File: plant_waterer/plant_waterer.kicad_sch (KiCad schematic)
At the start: 26 parts, among them J1 Conn_01x02, J2 Conn_01x02, J3 PJ-002AH, J4 Conn_01x03, U1 TB6612FNG,C,8,EL, U2 OLED_DISP, U3 XIAO_RP2040, U4 ESD7002, U5 AP2204R-5.0TRG1

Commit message: Switched pot to ADC pin
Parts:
- removed R1: 10K, Resistor_SMD:R_0805_2012Metric_Pad1.20x1.40mm_HandSolder, symbol Device:R
- removed RV1: 100K, Connector_PinHeader_2.54mm:PinHeader_1x03_P2.54mm_Vertical, symbol Device:Varistor
- added RV1: R_Potentiometer, Potentiometer_THT:Potentiometer_Bourns_3266Y_Vertical, symbol Device:R_Potentiometer
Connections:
- net +3.3V: now also RV1.1
- net GND: now also RV1.3
- net PWMA: now also U3.7 (CSn); no longer U3.1 (A1)
- new net: RV1.2, U3.1 (A1)
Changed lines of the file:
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@@
   (junction (at 90.17 48.26) (diameter 0) (color 0 0 0 0)
   )
-  (junction (at 115.57 137.16) (diameter 0) (color 0 0 0 0)
-  )
   (junction (at 250.19 102.87) (diameter 0) (color 0 0 0 0)
   )
@@
     (stroke (width 0) (type default) (color 0 0 0 0))
   )
-  (wire (pts (xy 107.95 133.35) (xy 107.95 137.16))
-    (stroke (width 0) (type default) (color 0 0 0 0))
-  )
   (wire (pts (xy 96.52 48.26) (xy 105.41 48.26))
     (stroke (width 0) (type default) (color 0 0 0 0))
@@
     (stroke (width 0) (type default) (color 0 0 0 0))
   )
-  (wire (pts (xy 115.57 148.59) (xy 115.57 151.13))
+  (wire (pts (xy 115.57 133.35) (xy 115.57 135.89))
     (stroke (width 0) (type default) (color 0 0 0 0))
   )
@@
     (stroke (width 0) (type default) (color 0 0 0 0))
   )
+  (wire (pts (xy 111.76 129.54) (xy 110.49 129.54))
+    (stroke (width 0) (type default) (color 0 0 0 0))
+  )
   (wire (pts (xy 148.59 29.21) (xy 148.59 31.75))
     (stroke (width 0) (type default) (color 0 0 0 0))
@@
     (stroke (width 0) (type default) (color 0 0 0 0))
   )
+  (wire (pts (xy 78.74 120.65) (xy 78.74 137.16))
+    (stroke (width 0) (type default) (color 0 0 0 0))
+  )
   (wire (pts (xy 54.61 31.75) (xy 59.69 31.75))
     (stroke (width 0) (type default) (color 0 0 0 0))
@@
     (stroke (width 0) (type default) (color 0 0 0 0))
   )
-  (wire (pts (xy 115.57 133.35) (xy 115.57 137.16))
+  (wire (pts (xy 110.49 129.54) (xy 110.49 137.16))
     (stroke (width 0) (type default) (color 0 0 0 0))
   )
@@
     (stroke (width 0) (type default) (color 0 0 0 0))
   )
+  (wire (pts (xy 110.49 137.16) (xy 78.74 137.16))
+    (stroke (width 0) (type default) (color 0 0 0 0))
+  )
   (polyline (pts (xy 158.75 87.63) (xy 264.16 87.63))
     (stroke (width 0) (type default) (color 0 0 0 0))
@@
     (stroke (width 0) (type default) (color 0 0 0 0))
   )
-  (wire (pts (xy 102.87 133.35) (xy 107.95 133.35))
-    (stroke (width 0) (type default) (color 0 0 0 0))
-  )
   (wire (pts (xy 43.18 31.75) (xy 43.18 35.56))
     (stroke (width 0) (type default) (color 0 0 0 0))
@@
     (stroke (width 0) (type default) (color 0 0 0 0))
   )
-  (wire (pts (xy 115.57 137.16) (xy 115.57 140.97))
-    (stroke (width 0) (type default) (color 0 0 0 0))
-  )
   (wire (pts (xy 90.17 48.26) (xy 96.52 48.26))
     (stroke (width 0) (type default) (color 0 0 0 0))
@@
     (stroke (width 0) (type default) (color 0 0 0 0))
   )
-  (wire (pts (xy 107.95 137.16) (xy 115.57 137.16))
-    (stroke (width 0) (type default) (color 0 0 0 0))
-  )
   (wire (pts (xy 256.54 115.57) (xy 256.54 116.84))
     (stroke (width 0) (type default) (color 0 0 0 0))
@@
     (stroke (width 0) (type default) (color 0 0 0 0))
   )
-  (wire (pts (xy 81.28 120.65) (xy 87.63 120.65))
+  (wire (pts (xy 78.74 120.65) (xy 87.63 120.65))
     (stroke (width 0) (type default) (color 0 0 0 0))
   )
@@
     (stroke (width 0) (type default) (color 0 0 0 0))
   )
+  (wire (pts (xy 102.87 133.35) (xy 104.14 133.35))
+    (stroke (width 0) (type default) (color 0 0 0 0))
+  )
   (wire (pts (xy 39.37 31.75) (xy 43.18 31.75))
     (stroke (width 0) (type default) (color 0 0 0 0))
@@
     (effects (font (size 1.27 1.27)) (justify left bottom))
   )
-  (label "PWMA" (at 81.28 120.65 0)
-    (effects (font (size 1.27 1.27)) (justify left bottom))
-  )
   (label "AIN2" (at 104.14 128.27 0)
     (effects (font (size 1.27 1.27)) (justify left bottom))
@@
   )
   (label "BIN1" (at 81.28 123.19 0)
+    (effects (font (size 1.27 1.27)) (justify left bottom))
+  )
+  (label "PWMA" (at 104.14 133.35 0)
     (effects (font (size 1.27 1.27)) (justify left bottom))
   )
@@
     (pin "1")
   )
+  (symbol (lib_id "Device:R_Potentiometer") (at 115.57 129.54 0) (mirror y) (unit 1)
+    (in_bom yes) (on_board yes)
+    (property "Reference" "RV1" (id 0) (at 118.11 128.2699 0)
+      (effects (font (size 1.27 1.27)) (justify right))
+    )
+    (property "Value" "R_Potentiometer" (id 1) (at 116.84 137.16 0)
+      (effects (font (size 1.27 1.27)) (justify right) hide)
+    )
+    (property "Footprint" "Potentiometer_THT:Potentiometer_Bourns_3266Y_Vertical" (id 2) (at 115.57 129.54 0)
+      (effects (font (size 1.27 1.27)) hide)
+    )
+    (property "Datasheet" "~" (id 3) (at 115.57 129.54 0)
+      (effects (font (size 1.27 1.27)) hide)
+    )
+    (pin "1")
+    (pin "2")
+    (pin "3")
+  )
   (symbol (lib_id "power:GND") (at 78.74 154.94 0) (unit 1)
     (in_bom yes) (on_board yes) (fields_autoplaced)
@@
     )
     (pin "1")
-  )
-  (symbol (lib_id "Device:R") (at 115.57 144.78 0) (unit 1)
-    (in_bom yes) (on_board yes) (fields_autoplaced)
-    (property "Reference" "R1" (id 0) (at 118.11 143.5099 0)
-      (effects (font (size 1.27 1.27)) (justify left))
-    )
-    (property "Value" "10K" (id 1) (at 118.11 146.0499 0)
-      (effects (font (size 1.27 1.27)) (justify left))
-    )
-    (property "Footprint" "Resistor_SMD:R_0805_2012Metric_Pad1.20x1.40mm_HandSolder" (id 2) (at 113.792 144.78 90)
-      (effects (font (size 1.27 1.27)) hide)
-    )
-    (property "Datasheet" "~" (id 3) (at 115.57 144.78 0)
-      (effects (font (size 1.27 1.27)) hide)
-    )
-    (pin "1")
-    (pin "2")
   )
   (symbol (lib_id "Device:C") (at 83.82 38.1 180) (unit 1)
@@
     (pin "1")
   )
-  (symbol (lib_id "power:GND") (at 115.57 151.13 0) (unit 1)
-    (in_bom yes) (on_board yes) (fields_autoplaced)
-    (property "Reference" "#PWR0105" (id 0) (at 115.57 157.48 0)
-      (effects (font (size 1.27 1.27)) hide)
-    )
-    (property "Value" "GND" (id 1) (at 115.57 156.21 0))
-    (property "Footprint" "" (id 2) (at 115.57 151.13 0)
-      (effects (font (size 1.27 1.27)) hide)
-    )
-    (property "Datasheet" "" (id 3) (at 115.57 151.13 0)
-      (effects (font (size 1.27 1.27)) hide)
-    )
-    (pin "1")
-  )
-  (symbol (lib_id "Device:Varistor") (at 115.57 129.54 0) (unit 1)
-    (in_bom yes) (on_board yes) (fields_autoplaced)
-    (property "Reference" "RV1" (id 0) (at 118.11 128.5231 0)
-      (effects (font (size 1.27 1.27)) (justify left))
-    )
-    (property "Value" "100K" (id 1) (at 118.11 131.0631 0)
-      (effects (font (size 1.27 1.27)) (justify left))
-    )
-    (property "Footprint" "Connector_PinHeader_2.54mm:PinHeader_1x03_P2.54mm_Vertical" (id 2) (at 113.792 129.54 90)
-      (effects (font (size 1.27 1.27)) hide)
-    )
-    (property "Datasheet" "~" (id 3) (at 115.57 129.54 0)
-      (effects (font (size 1.27 1.27)) hide)
-    )
-    (pin "1")
-    (pin "2")
+  (symbol (lib_id "power:GND") (at 115.57 135.89 0) (unit 1)
+    (in_bom yes) (on_board yes) (fields_autoplaced)
+    (property "Reference" "#PWR0105" (id 0) (at 115.57 142.24 0)
+      (effects (font (size 1.27 1.27)) hide)
+    )
+    (property "Value" "GND" (id 1) (at 115.57 140.97 0))
+    (property "Footprint" "" (id 2) (at 115.57 135.89 0)
+      (effects (font (size 1.27 1.27)) hide)
+    )
+    (property "Datasheet" "" (id 3) (at 115.57 135.89 0)
+      (effects (font (size 1.27 1.27)) hide)
+    )
+    (pin "1")
   )
   (symbol (lib_id "Device:R") (at 68.58 123.19 0) (unit 1)
@@
       (reference "JP1") (unit 1) (value "Jumper_2_Bridged") (footprint "Connector_PinHeader_2.54mm:PinHeader_1x02_P2.54mm_Vertical")
     )
-    (path "/3db4251a-e88f-41da-b4ca-02be30b2764f"
-      (reference "R1") (unit 1) (value "10K") (footprint "Resistor_SMD:R_0805_2012Metric_Pad1.20x1.40mm_HandSolder")
-    )
     (path "/12cb9a3a-0dce-4456-8425-08803bf20070"
       (reference "R2") (unit 1) (value "10K") (footprint "Resistor_SMD:R_0805_2012Metric_Pad1.20x1.40mm_HandSolder")
@@
       (reference "R3") (unit 1) (value "10K") (footprint "Resistor_SMD:R_0805_2012Metric_Pad1.20x1.40mm_HandSolder")
     )
-    (path "/b008a221-6b1c-4862-b6b9-3bd19966dc9e"
-      (reference "RV1") (unit 1) (value "100K") (footprint "Connector_PinHeader_2.54mm:PinHeader_1x03_P2.54mm_Vertical")
+    (path "/2dee0ead-6279-42da-9328-a22cafe0f3c3"
+      (reference "RV1") (unit 1) (value "R_Potentiometer") (footprint "Potentiometer_THT:Potentiometer_Bourns_3266Y_Vertical")
     )
     (path "/032b3c9e-8639-45d6-8bdd-7a89ce998692"

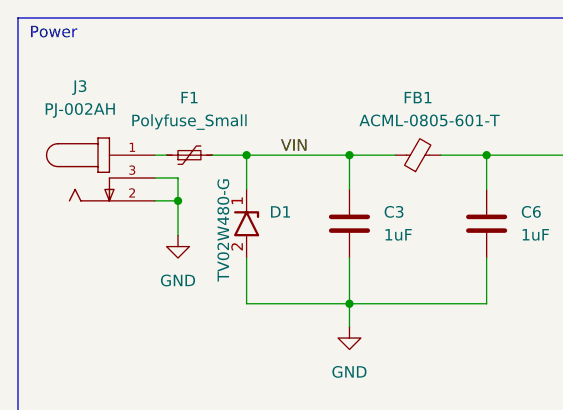
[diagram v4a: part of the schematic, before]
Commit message: V7 pre-switch to RPi-Pico
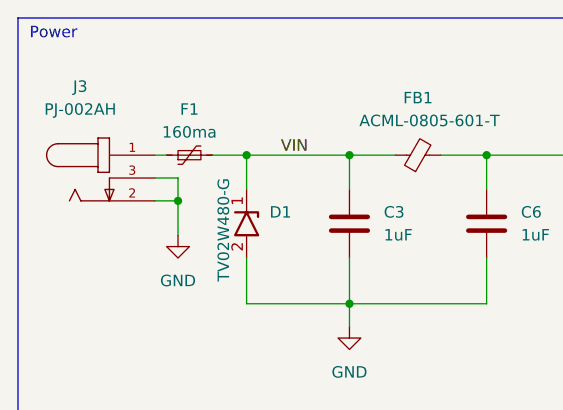
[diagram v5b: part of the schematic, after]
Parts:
- F1: value Polyfuse_Small -> 160ma

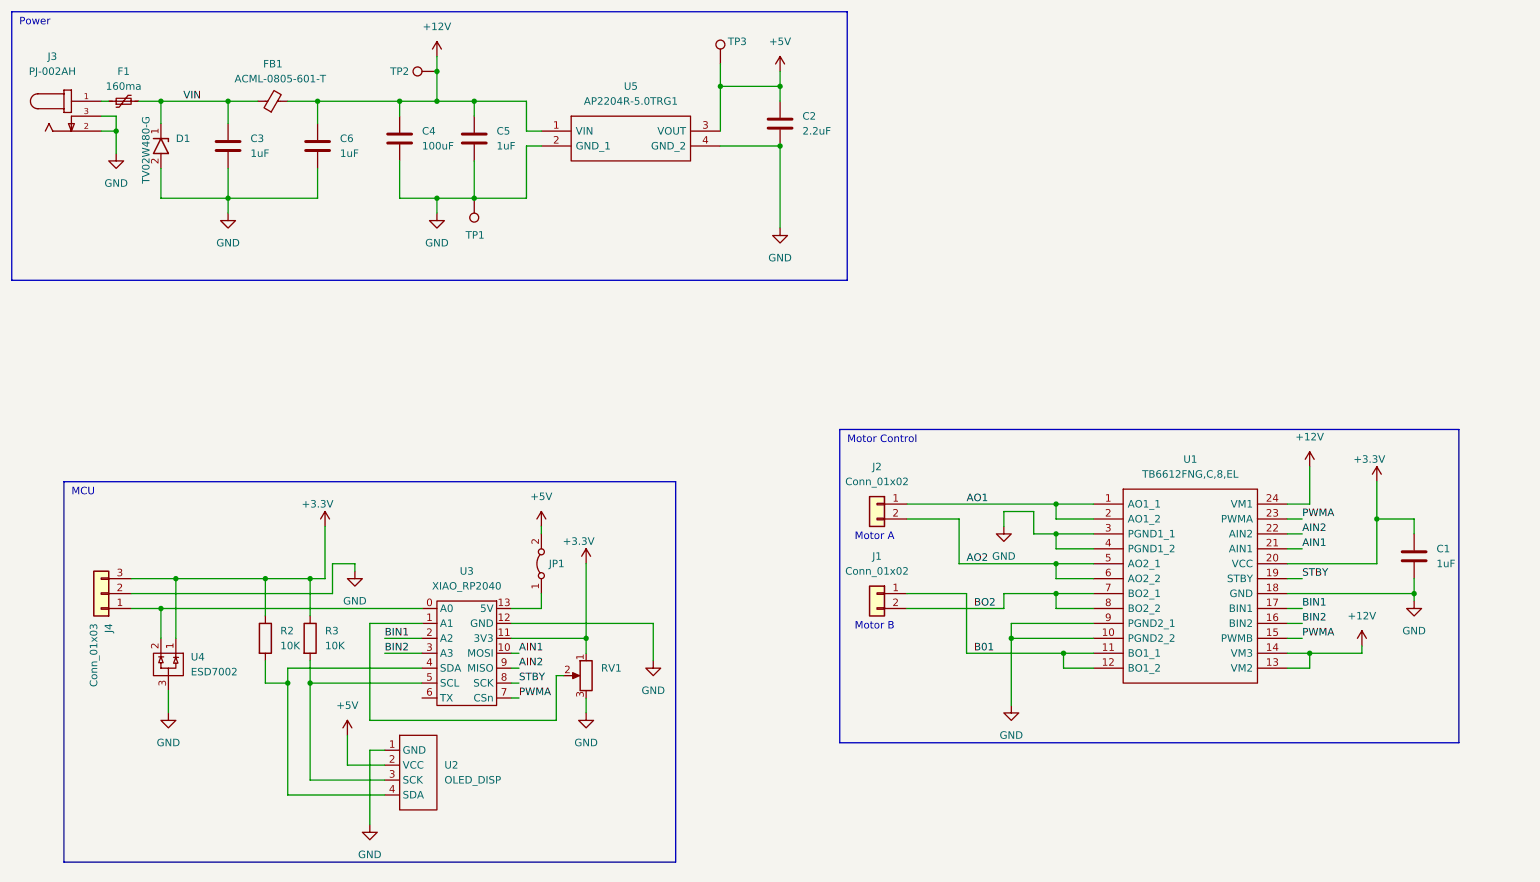
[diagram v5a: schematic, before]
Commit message: Swapped in RPi Pico W
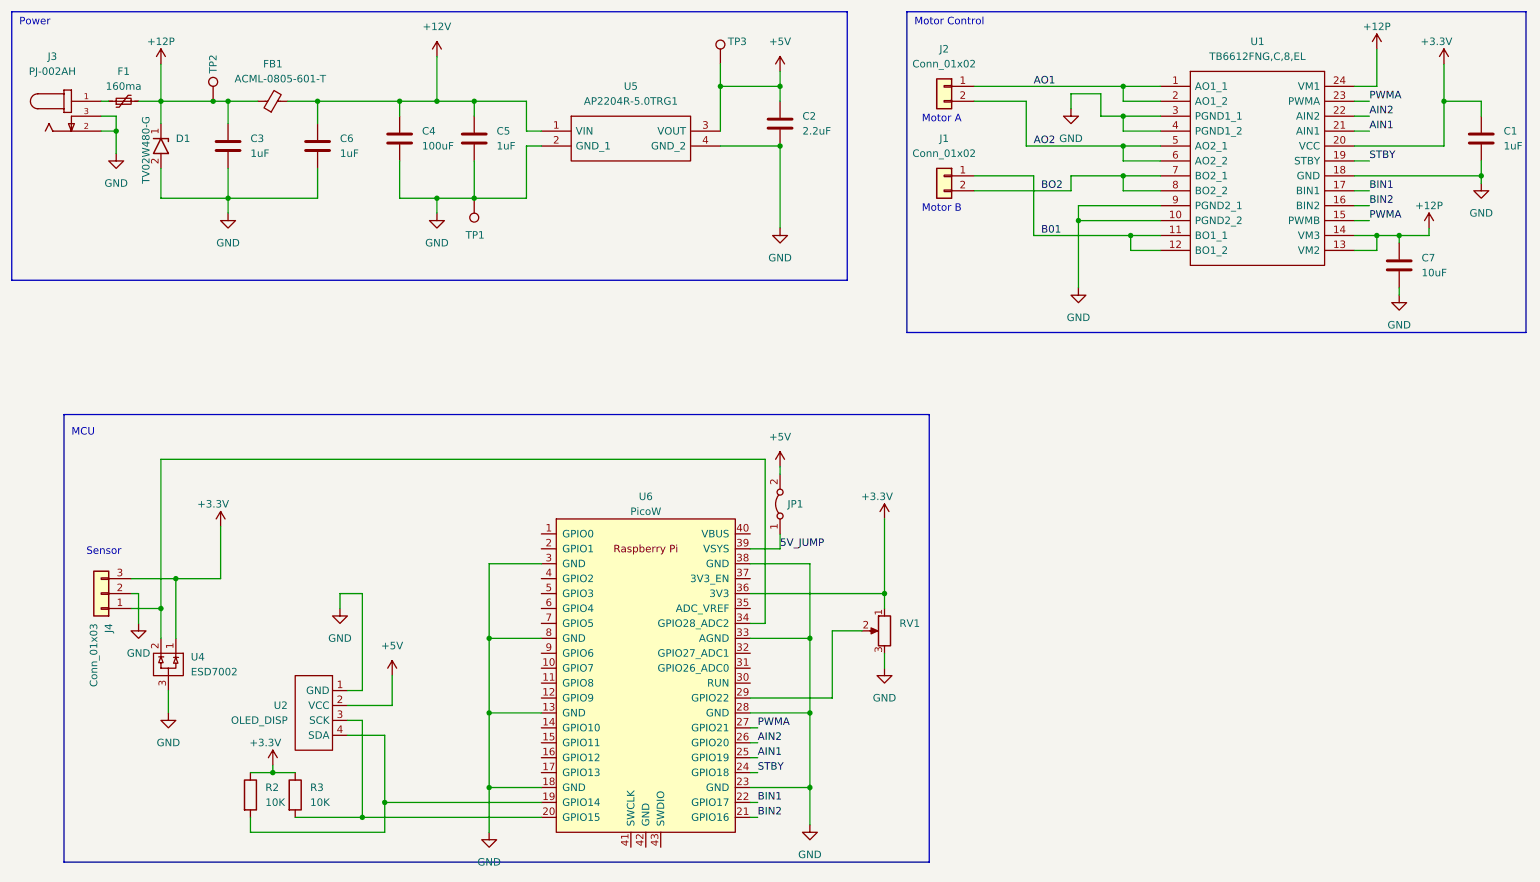
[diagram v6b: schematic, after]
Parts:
- removed U3: XIAO_RP2040, Library:XIAO RP2040, symbol MySymbols:XIAO_RP2040
- added C7: 10uF, Capacitor_SMD:C_0805_2012Metric_Pad1.18x1.45mm_HandSolder, symbol Device:C
- added U6: PicoW, RPi_Pico:RPi_PicoW_SMD_TH, symbol RPi_Pico:PicoW
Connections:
- net +12V: no longer TP2.1, U1.13 (VM2), U1.14 (VM3), U1.24 (VM1)
- net +3.3V: now also U6.36 (3V3)
- net AIN1: now also U6.25 (GPIO19)
- net AIN2: now also U6.26 (GPIO20)
- net BIN1: now also U6.22 (GPIO17)
- net BIN2: now also U6.21 (GPIO16)
- net GND: now also C7.1, U6.13 (GND), U6.18 (GND), U6.23 (GND), U6.28 (GND), U6.3 (GND), U6.33 (AGND), U6.38 (GND), U6.8 (GND)
- net PWMA: now also U6.27 (GPIO21)
- net STBY: now also U6.24 (GPIO18)
- net at R2.2, U2.4 (SDA): now also U6.19 (GPIO14)
- net at RV1.2: now also U6.29 (GPIO22)
- net at J4.1 (Pin_1), U4.2: now also U6.34 (GPIO28_ADC2)
- net 5V_JUMP: now reaches JP1.1 (A)
- net 5V_JUMP: now also U6.39 (VSYS)
- net at R3.2, U2.3 (SCK): now also U6.20 (GPIO15)
- net VIN renamed +12P
- net +12P: now also TP2.1, U1.13 (VM2), U1.14 (VM3), U1.24 (VM1), C7.2
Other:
- note added: "Sensor"
- moved on the sheet: C1, J1, J2, JP1, R2, R3, RV1, U1, U2

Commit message: Switched to different motor driver ZXBM5210-SP-13
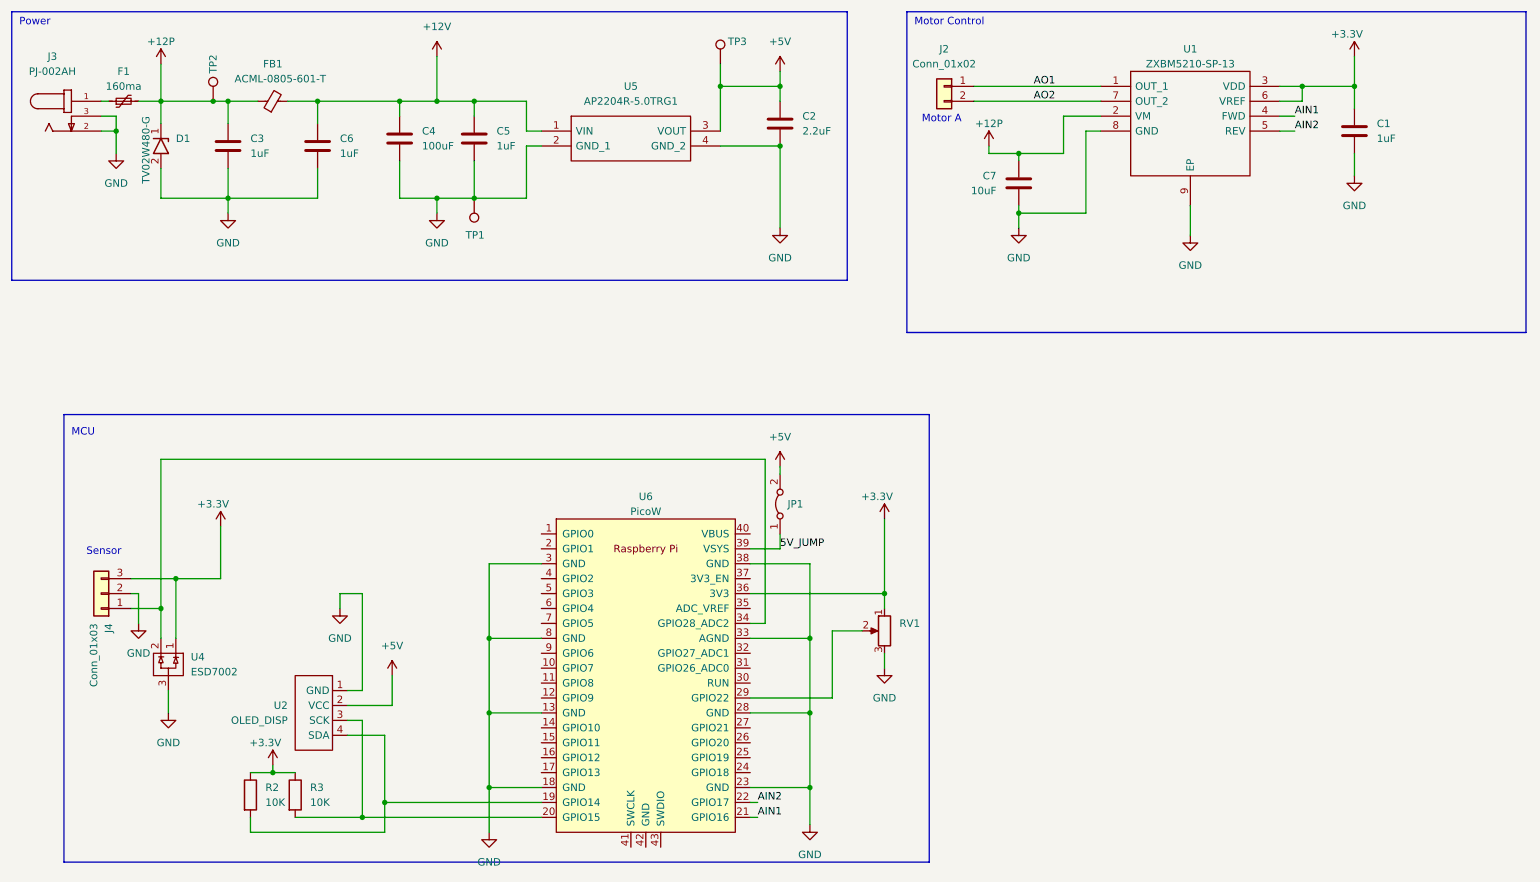
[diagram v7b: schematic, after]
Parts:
- removed J1: Conn_01x02, Library:CONN 1x2 5mm, symbol Connector_Generic:Conn_01x02
- removed U1: TB6612FNG,C,8,EL, Library:SOP65P760X160-24N, symbol MySymbols:TB6612FNG,C,8,EL
- added U1: ZXBM5210-SP-13, Package_SO:SOIC-8-1EP_3.9x4.9mm_P1.27mm_EP2.41x3.81mm_ThermalVias, symbol MySymbols:ZXBM5210-SP-13
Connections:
- net BIN1 is gone; now on net AIN2: U6.22 (GPIO17)
- net BIN2 is gone; now on net AIN1: U6.21 (GPIO16)
- net +12P: now also U1.2 (VM)
- net +3.3V: now also U1.3 (VDD), U1.6 (VREF)
- net AIN1: now also U1.4 (FWD); no longer U6.25 (GPIO19)
- net AIN2: now also U1.5 (REV); no longer U6.26 (GPIO20)
- net AO1: now also U1.1 (OUT_1)
- net AO2: now also U1.7 (OUT_2)
- net GND: now also U1.8 (GND), U1.9 (EP)
- net PWMA: no longer names the net of U6.27 (GPIO21)
- net STBY: no longer names the net of U6.24 (GPIO18)
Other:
- note removed: "Motor B"
- moved on the sheet: C1, C7
